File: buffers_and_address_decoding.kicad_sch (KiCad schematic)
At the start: 32 parts, among them U17 LS30, U18 74LS283, U19 LS04, U27 ADDR SELECT, U28 74LS283, U29 LS10, U3 81LS95, U30 LS20, U37 LS04, U38 LS10, U39 LS00, U4 LS04, U40 74LS42, U47 VECTOR FETCH ENAB, U7 LS30, U8 LS30

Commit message: First version of the schematic completed
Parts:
- U17: symbol 74LS30:74LS30_U17 -> LS_Logic:74LS30_U17
- U18, U28: symbol 74LS283:74LS283 -> LS_Logic:74LS283
- U3: symbol 81LS95:81LS95 -> LS_Logic:81LS95
- U37: footprint Package_DIP:DIP-14_W7.62mm_LongPads -> (none)
- U40: symbol 74LS42:74LS42_U40 -> LS_Logic:74LS42_U40
- U47: value VECTOR FETCH ENAB -> SYST
- U7: symbol 74LS30:74LS30_U7 -> LS_Logic:74LS30_U7
- U8: symbol 74LS30:74LS30_U8 -> LS_Logic:74LS30_U8
- renumbered R8 to R1, R3 to R10, R6 to R2, R4 to R3, R2 to R4, R5 to R7, R7 to R8, R1 to R9
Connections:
- net AB_0 renamed AB0
- net AB_1 renamed AB1
- net AB_10 renamed AB10
- net AB_11 renamed AB11
- net AB_12 renamed AB12
- net AB_13 renamed AB13
- net AB_14 renamed AB14
- net AB_15 renamed AB15
- net AB_2 renamed AB2
- net AB_3 renamed AB3
- net AB_4 renamed AB4
- net AB_5 renamed AB5
- net AB_6 renamed AB6
- net AB_7 renamed AB7
- net AB_8 renamed AB8
- net AB_9 renamed AB9
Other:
- note added: "VECTOR FETCH ENAB"
- note removed: "SYST"

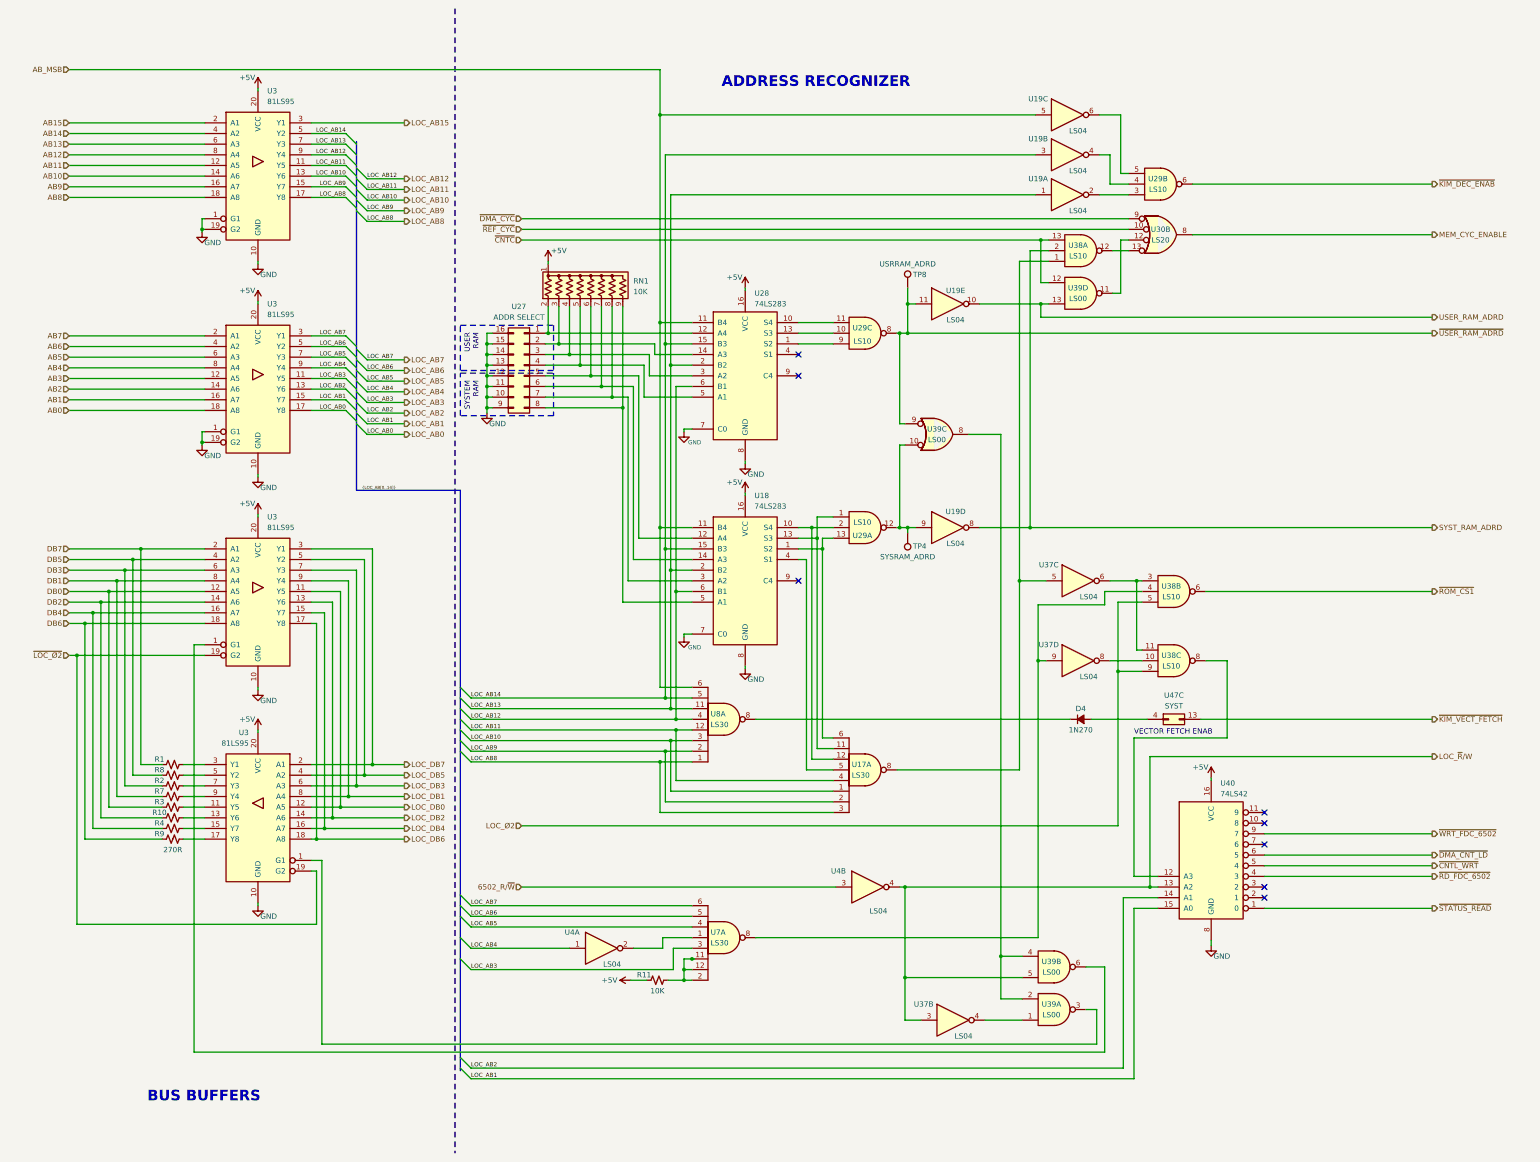
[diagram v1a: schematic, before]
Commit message: Schematic corrections
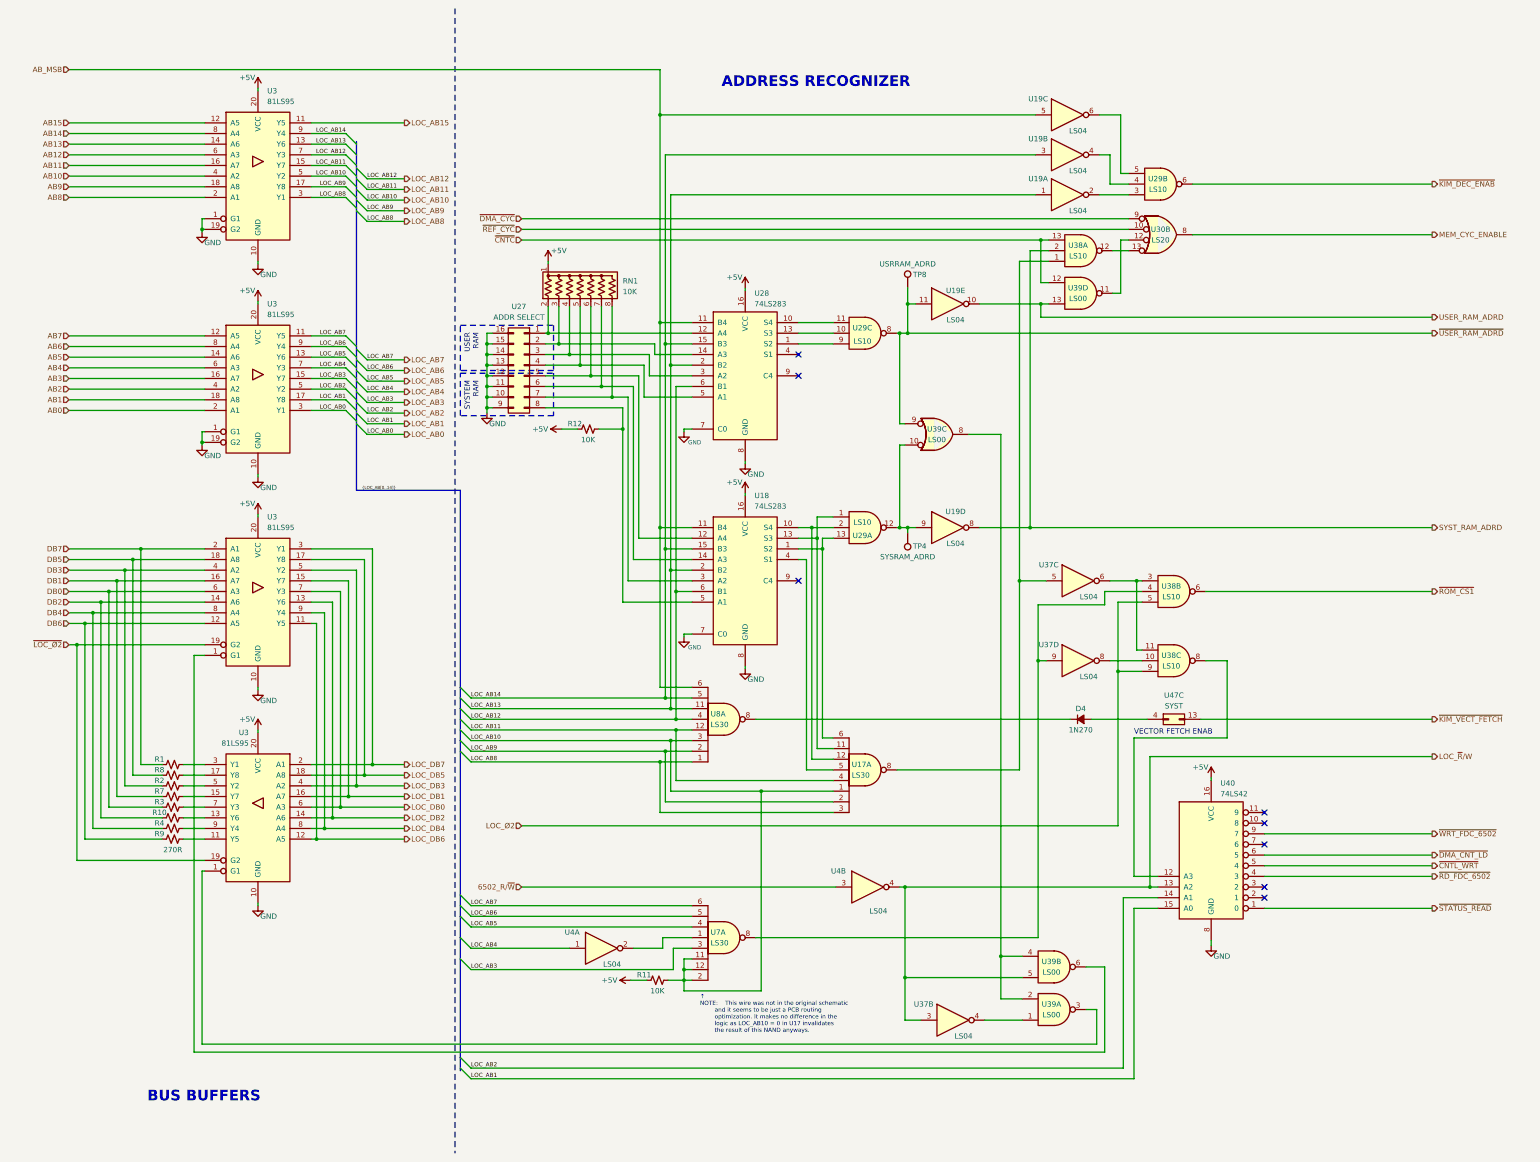
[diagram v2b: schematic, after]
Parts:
- added R12: 10K, K_1013_Jumper:R_Axial_DIN0204_L3.6mm_D2.5mm_P12.70mm_Horizontal, symbol Device:R_Small_US
- D4: footprint Diode_THT:D_DO-35_SOD27_P7.62mm_Horizontal -> K_1013_Jumper:D_DO-35_SOD27_P12.70mm_Horizontal
- R1, R10, R11, R2, R3, R4, R7, R8, R9: footprint Resistor_THT:R_Axial_DIN0207_L6.3mm_D2.5mm_P10.16mm_Horizontal -> K_1013_Jumper:R_Axial_DIN0204_L3.6mm_D2.5mm_P12.70mm_Horizontal
- RN1: footprint Resistor_THT:R_Array_SIP9 -> K_1013_Jumper:R_Array_SIP8; symbol Device:R_Network08_US -> Device:R_Network07_US
- TP4, TP8: footprint (none) -> K_1013_Jumper:TestPoint
- U17, U19, U29, U30, U38, U39, U4, U7, U8: footprint Package_DIP:DIP-14_W7.62mm_LongPads -> K_1013_Jumper:DIP-14_W7.62mm_LongPads
- U18, U27, U28, U47: footprint Package_DIP:DIP-16_W7.62mm_Socket_LongPads -> K_1013_Jumper:DIP-16_W7.62mm_LongPads
- U3: footprint Package_DIP:DIP-20_W7.62mm_LongPads -> K_1013_Jumper:DIP-20_W7.62mm_LongPads
- U3: footprint Package_DIP:DIP-20_W7.62mm_LongPads -> K_1013_Jumper:DIP-20_W7.62mm_LongPads; symbol LS_Logic:81LS95 -> LS_Logic:81LS95_U9
- U3: footprint Package_DIP:DIP-20_W7.62mm_LongPads -> K_1013_Jumper:DIP-20_W7.62mm_LongPads; symbol LS_Logic:81LS95 -> LS_Logic:81LS95_U3
- U37: footprint (none) -> K_1013_Jumper:DIP-14_W7.62mm_LongPads
- U40: footprint Package_DIP:DIP-16_W7.62mm_LongPads -> K_1013_Jumper:DIP-16_W7.62mm_LongPads
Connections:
- net +5V: now also R12.1
- net AB0: now also U3.2 (A1); no longer U3.18 (A8)
- net AB1: now also U3.18 (A8); no longer U3.16 (A7)
- net AB10: now also U3.4 (A2); no longer U3.14 (A6)
- net AB11: now also U3.16 (A7); no longer U3.12 (A5)
- net AB12: now also U3.6 (A3); no longer U3.8 (A4)
- net AB13: now also U3.14 (A6); no longer U3.6 (A3)
- net AB14: now also U3.8 (A4); no longer U3.4 (A2)
- net AB15: now also U3.12 (A5); no longer U3.2 (A1)
- net AB2: now also U3.4 (A2); no longer U3.14 (A6)
- net AB3: now also U3.16 (A7); no longer U3.12 (A5)
- net AB4: now also U3.6 (A3); no longer U3.8 (A4)
- net AB5: now also U3.14 (A6); no longer U3.6 (A3)
- net AB6: now also U3.8 (A4); no longer U3.4 (A2)
- net AB7: now also U3.12 (A5); no longer U3.2 (A1)
- net AB8: now also U3.2 (A1); no longer U3.18 (A8)
- net AB9: now also U3.18 (A8); no longer U3.16 (A7)
- net DB0: now also U3.6 (A3); no longer U3.12 (A5)
- net DB1: now also U3.16 (A7); no longer U3.8 (A4)
- net DB3: now also U3.4 (A2); no longer U3.6 (A3)
- net DB4: now also U3.8 (A4); no longer U3.16 (A7)
- net DB5: now also U3.18 (A8); no longer U3.4 (A2)
- net DB6: now also U3.12 (A5); no longer U3.18 (A8)
- net LOC_AB0: now also U3.3 (Y1); no longer U3.17 (Y8)
- net LOC_AB1: now also U3.17 (Y8); no longer U3.15 (Y7)
- net LOC_AB10: now also R11.2, U3.5 (Y2), U7.11, U7.12, U7.2; no longer U3.13 (Y6)
- net LOC_AB11: now also U3.15 (Y7); no longer U3.11 (Y5)
- net LOC_AB12: now also U3.7 (Y3); no longer U3.9 (Y4)
- net LOC_AB13: now also U3.13 (Y6); no longer U3.7 (Y3)
- net LOC_AB14: now also U3.9 (Y4); no longer U3.5 (Y2)
- net LOC_AB15: now also U3.11 (Y5); no longer U3.3 (Y1)
- net LOC_AB2: now also U3.5 (Y2); no longer U3.13 (Y6)
- net LOC_AB3: now also U3.15 (Y7); no longer U3.11 (Y5)
- net LOC_AB4: now also U3.7 (Y3); no longer U3.9 (Y4)
- net LOC_AB5: now also U3.13 (Y6); no longer U3.7 (Y3)
- net LOC_AB6: now also U3.9 (Y4); no longer U3.5 (Y2)
- net LOC_AB7: now also U3.11 (Y5); no longer U3.3 (Y1)
- net LOC_AB8: now also U3.3 (Y1); no longer U3.17 (Y8)
- net LOC_AB9: now also U3.17 (Y8); no longer U3.15 (Y7)
- net LOC_DB0: now also U3.6 (A3), U3.7 (Y3); no longer U3.11 (Y5), U3.12 (A5)
- net LOC_DB1: now also U3.15 (Y7), U3.16 (A7); no longer U3.8 (A4), U3.9 (Y4)
- net LOC_DB3: now also U3.4 (A2), U3.5 (Y2); no longer U3.6 (A3), U3.7 (Y3)
- net LOC_DB4: now also U3.8 (A4), U3.9 (Y4); no longer U3.15 (Y7), U3.16 (A7)
- net LOC_DB5: now also U3.17 (Y8), U3.18 (A8); no longer U3.4 (A2), U3.5 (Y2)
- net LOC_DB6: now also U3.11 (Y5), U3.12 (A5); no longer U3.17 (Y8), U3.18 (A8)
- net at R7.2: now also U3.15 (Y7); no longer U3.9 (Y4)
- net at R8.2: now also U3.17 (Y8); no longer U3.5 (Y2)
- net at U18.5 (A1), U27.8 (Pin_8): now also R12.2; no longer RN1.9 (R8)
- net at U3.11 (Y5): now also R9.2; no longer R3.2
- net at R4.2: now also U3.9 (Y4); no longer U3.15 (Y7)
- net at R2.2: now also U3.5 (Y2); no longer U3.7 (Y3)
- new net: R3.2, U3.7 (Y3)
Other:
- note added: "↑ NOTE: This wire was not in the original schematic and it seems to be just a PCB routing optimization. It makes no difference in the logic as LOC_AB10 = 0 in U17 invalidates the result of this NAND anyways."

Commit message: Update progress
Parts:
- D4: footprint K_1013_Jumper:D_DO-35_SOD27_P12.70mm_Horizontal -> K_1013:D_DO-35_SOD27_P12.70mm_Horizontal
- R1, R10, R11, R12, R2, R3, R4, R7, R8, R9: footprint K_1013_Jumper:R_Axial_DIN0204_L3.6mm_D2.5mm_P12.70mm_Horizontal -> K_1013:R_Axial_DIN0204_L3.6mm_D2.5mm_P12.70mm_Horizontal
- RN1: footprint K_1013_Jumper:R_Array_SIP8 -> K_1013:R_Array_SIP8
- TP4, TP8: footprint K_1013_Jumper:TestPoint -> K_1013:TestPoint
- U17, U29, U30, U37, U38, U39, U4, U7, U8: footprint K_1013_Jumper:DIP-14_W7.62mm_LongPads -> K_1013:DIP-14_W7.62mm_LongPads
- U18, U27, U28, U40, U47: footprint K_1013_Jumper:DIP-16_W7.62mm_LongPads -> K_1013:DIP-16_W7.62mm_LongPads
- U19: footprint K_1013_Jumper:DIP-14_W7.62mm_LongPads -> K_1013:DIP-14_W7.62mm_LongPads_U19
- U3: footprint K_1013_Jumper:DIP-20_W7.62mm_LongPads -> K_1013:DIP-20_W7.62mm_LongPads; symbol LS_Logic:81LS95 -> LS_Logic:81LS95_U1_U2
- U3: footprint K_1013_Jumper:DIP-20_W7.62mm_LongPads -> K_1013:DIP-20_W7.62mm_LongPads_U9
- U3: footprint K_1013_Jumper:DIP-20_W7.62mm_LongPads -> K_1013:DIP-20_W7.62mm_LongPads
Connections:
- net DB0: now also R9.1, U3.12 (A5); no longer R3.1, U3.6 (A3)
- net DB1: now also R4.1, U3.8 (A4); no longer R7.1, U3.16 (A7)
- net DB3: now also R3.1, U3.6 (A3); no longer R2.1, U3.4 (A2)
- net DB4: now also R7.1, U3.16 (A7); no longer R4.1, U3.8 (A4)
- net DB5: now also R2.1, U3.4 (A2); no longer R8.1, U3.18 (A8)
- net DB6: now also R8.1, U3.18 (A8); no longer R9.1, U3.12 (A5)
- net LOC_DB0: now also U3.11 (Y5), U3.12 (A5); no longer U3.6 (A3), U3.7 (Y3)
- net LOC_DB1: now also U3.8 (A4), U3.9 (Y4); no longer U3.15 (Y7), U3.16 (A7)
- net LOC_DB3: now also U3.6 (A3), U3.7 (Y3); no longer U3.4 (A2), U3.5 (Y2)
- net LOC_DB4: now also U3.15 (Y7), U3.16 (A7); no longer U3.8 (A4), U3.9 (Y4)
- net LOC_DB5: now also U3.4 (A2), U3.5 (Y2); no longer U3.17 (Y8), U3.18 (A8)
- net LOC_DB6: now also U3.17 (Y8), U3.18 (A8); no longer U3.11 (Y5), U3.12 (A5)

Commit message: Routing of the bottom layer completed
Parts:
- U17: footprint K_1013:DIP-14_W7.62mm_LongPads -> K_1013:DIP-14_W7.62mm_LongPads_U17
- U30: footprint K_1013:DIP-14_W7.62mm_LongPads -> K_1013:DIP-14_W7.62mm_LongPads_U30
- U37: footprint K_1013:DIP-14_W7.62mm_LongPads -> K_1013:DIP-14_W7.62mm_LongPads_U37
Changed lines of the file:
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@@
       (effects (font (size 1.27 1.27)))
     )
-    (property "Footprint" "K_1013:DIP-14_W7.62mm_LongPads" (at 280.035 148.59 0)
+    (property "Footprint" "K_1013:DIP-14_W7.62mm_LongPads_U37" (at 280.035 148.59 0)
       (effects (font (size 1.27 1.27)) hide)
     )
@@
       (effects (font (size 1.27 1.27)))
     )
-    (property "Footprint" "K_1013:DIP-14_W7.62mm_LongPads" (at 299.72 66.04 0)
+    (property "Footprint" "K_1013:DIP-14_W7.62mm_LongPads_U30" (at 299.72 66.04 0)
       (effects (font (size 1.27 1.27)) hide)
     )
@@
       (effects (font (size 1.27 1.27)) (justify left))
     )
-    (property "Footprint" "K_1013:DIP-14_W7.62mm_LongPads" (at 229.235 193.675 0)
+    (property "Footprint" "K_1013:DIP-14_W7.62mm_LongPads_U17" (at 229.235 193.675 0)
       (effects (font (size 1.27 1.27)) hide)
     )
@@
       (effects (font (size 1.27 1.27)))
     )
-    (property "Footprint" "K_1013:DIP-14_W7.62mm_LongPads" (at 280.035 167.64 0)
+    (property "Footprint" "K_1013:DIP-14_W7.62mm_LongPads_U37" (at 280.035 167.64 0)
       (effects (font (size 1.27 1.27)) hide)
     )
@@
       (effects (font (size 1.27 1.27)))
     )
-    (property "Footprint" "K_1013:DIP-14_W7.62mm_LongPads" (at 250.19 253.365 0)
-      (effects (font (size 1.27 1.27)) hide)
-    )
+    (property "Footprint" "K_1013:DIP-14_W7.62mm_LongPads_U37" (at 250.19 253.365 0)
+      (effects (font (size 1.27 1.27)) hide)
+    )

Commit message: Completed first version of board routing
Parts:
- R1, R10, R2, R3, R4, R7, R8, R9: footprint K_1013:R_Axial_DIN0204_L3.6mm_D2.5mm_P12.70mm_Horizontal -> K_1013:R_Axial_DIN0204_L3.6mm_D2.5mm_P12.70mm_Horizontal_270R
- R11, R12: footprint K_1013:R_Axial_DIN0204_L3.6mm_D2.5mm_P12.70mm_Horizontal -> K_1013:R_Axial_DIN0204_L3.6mm_D2.5mm_P12.70mm_Horizontal_10K
- U27, U47: footprint K_1013:DIP-16_W7.62mm_LongPads -> K_1013:DIP-16_W7.62mm_LongPads_SW
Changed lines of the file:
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@@
       (effects (font (size 1.27 1.27)) hide)
     )
-    (property "Footprint" "K_1013:R_Axial_DIN0204_L3.6mm_D2.5mm_P12.70mm_Horizontal" (at 64.135 200.025 0)
+    (property "Footprint" "K_1013:R_Axial_DIN0204_L3.6mm_D2.5mm_P12.70mm_Horizontal_270R" (at 64.135 200.025 0)
       (effects (font (size 1.27 1.27)) hide)
     )
@@
       (effects (font (size 1.27 1.27)) hide)
     )
-    (property "Footprint" "K_1013:R_Axial_DIN0204_L3.6mm_D2.5mm_P12.70mm_Horizontal" (at 64.135 194.945 0)
+    (property "Footprint" "K_1013:R_Axial_DIN0204_L3.6mm_D2.5mm_P12.70mm_Horizontal_270R" (at 64.135 194.945 0)
       (effects (font (size 1.27 1.27)) hide)
     )
@@
       (effects (font (size 1.27 1.27)) hide)
     )
-    (property "Footprint" "K_1013:R_Axial_DIN0204_L3.6mm_D2.5mm_P12.70mm_Horizontal" (at 64.135 197.485 0)
+    (property "Footprint" "K_1013:R_Axial_DIN0204_L3.6mm_D2.5mm_P12.70mm_Horizontal_270R" (at 64.135 197.485 0)
       (effects (font (size 1.27 1.27)) hide)
     )
@@
       (effects (font (size 1.27 1.27)))
     )
-    (property "Footprint" "K_1013:R_Axial_DIN0204_L3.6mm_D2.5mm_P12.70mm_Horizontal" (at 179.705 243.84 0)
+    (property "Footprint" "K_1013:R_Axial_DIN0204_L3.6mm_D2.5mm_P12.70mm_Horizontal_10K" (at 179.705 243.84 0)
       (effects (font (size 1.27 1.27)) hide)
     )
@@
       (effects (font (size 1.27 1.27)) hide)
     )
-    (property "Footprint" "K_1013:R_Axial_DIN0204_L3.6mm_D2.5mm_P12.70mm_Horizontal" (at 64.135 205.105 0)
+    (property "Footprint" "K_1013:R_Axial_DIN0204_L3.6mm_D2.5mm_P12.70mm_Horizontal_270R" (at 64.135 205.105 0)
       (effects (font (size 1.27 1.27)) hide)
     )
@@
       (effects (font (size 1.27 1.27)))
     )
-    (property "Footprint" "K_1013:DIP-16_W7.62mm_LongPads" (at 147.955 97.155 0)
+    (property "Footprint" "K_1013:DIP-16_W7.62mm_LongPads_SW" (at 147.955 97.155 0)
       (effects (font (size 1.27 1.27)) hide)
     )
@@
       (effects (font (size 1.27 1.27)) hide)
     )
-    (property "Footprint" "K_1013:R_Axial_DIN0204_L3.6mm_D2.5mm_P12.70mm_Horizontal" (at 64.135 202.565 0)
+    (property "Footprint" "K_1013:R_Axial_DIN0204_L3.6mm_D2.5mm_P12.70mm_Horizontal_270R" (at 64.135 202.565 0)
       (effects (font (size 1.27 1.27)) hide)
     )
@@
       (effects (font (size 1.27 1.27)))
     )
-    (property "Footprint" "K_1013:R_Axial_DIN0204_L3.6mm_D2.5mm_P12.70mm_Horizontal" (at 163.195 112.395 0)
+    (property "Footprint" "K_1013:R_Axial_DIN0204_L3.6mm_D2.5mm_P12.70mm_Horizontal_10K" (at 163.195 112.395 0)
       (effects (font (size 1.27 1.27)) hide)
     )
@@
       (effects (font (size 1.27 1.27)) hide)
     )
-    (property "Footprint" "K_1013:R_Axial_DIN0204_L3.6mm_D2.5mm_P12.70mm_Horizontal" (at 64.135 207.645 0)
+    (property "Footprint" "K_1013:R_Axial_DIN0204_L3.6mm_D2.5mm_P12.70mm_Horizontal_270R" (at 64.135 207.645 0)
       (effects (font (size 1.27 1.27)) hide)
     )
@@
       (effects (font (size 1.27 1.27)))
     )
-    (property "Footprint" "K_1013:R_Axial_DIN0204_L3.6mm_D2.5mm_P12.70mm_Horizontal" (at 64.135 210.185 0)
+    (property "Footprint" "K_1013:R_Axial_DIN0204_L3.6mm_D2.5mm_P12.70mm_Horizontal_270R" (at 64.135 210.185 0)
       (effects (font (size 1.27 1.27)) hide)
     )
@@
       (effects (font (size 1.27 1.27)) hide)
     )
-    (property "Footprint" "K_1013:R_Axial_DIN0204_L3.6mm_D2.5mm_P12.70mm_Horizontal" (at 64.135 192.405 0)
+    (property "Footprint" "K_1013:R_Axial_DIN0204_L3.6mm_D2.5mm_P12.70mm_Horizontal_270R" (at 64.135 192.405 0)
       (effects (font (size 1.27 1.27)) hide)
     )
@@
       (effects (font (size 1.27 1.27)))
     )
-    (property "Footprint" "K_1013:DIP-16_W7.62mm_LongPads" (at 301.625 181.61 0)
-      (effects (font (size 1.27 1.27)) hide)
-    )
+    (property "Footprint" "K_1013:DIP-16_W7.62mm_LongPads_SW" (at 301.625 181.61 0)
+      (effects (font (size 1.27 1.27)) hide)
+    )

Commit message: Cosmetic changes
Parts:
- U30: symbol 74xx:74LS20 -> LS_Logic:74LS20_U30
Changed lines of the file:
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@@
     )
   )
-  (symbol (lib_id "LS_Logic:81LS95_U1_U2") (at 84.455 52.07 0) (unit 1)
+  (symbol (lib_name "81LS95_U1_U2_1") (lib_id "LS_Logic:81LS95_U1_U2") (at 84.455 52.07 0) (unit 1)
     (in_bom yes) (on_board yes) (dnp no)
     (property "Reference" "U3" (at 86.6491 31.75 0)
@@
     (pin "7")
     (pin "11")
+    (pin "10")
+    (pin "9")
+    (pin "13")
     (instances
       (project "k-1013-floppy-controller-replica"
@@
     )
   )
-  (symbol (lib_id "74xx:74LS20") (at 299.72 66.04 0) (unit 2) (convert 2)
+  (symbol (lib_id "LS_Logic:74LS20_U30") (at 299.72 66.04 0) (unit 2) (convert 2)
     (in_bom yes) (on_board yes) (dnp no)
     (property "Reference" "U30" (at 299.72 64.77 0)
@@
     (pin "7")
     (pin "2")
+    (pin "11")
     (instances
       (project "k-1013-floppy-controller-replica"
@@
     (pin "6")
     (pin "1")
+    (pin "10")
+    (pin "9")
+    (pin "13")
     (instances
       (project "k-1013-floppy-controller-replica"
@@
     (pin "9")
     (pin "10")
-    (instances
-      (project "k-1013-floppy-controller-replica"
+    (pin "13")
+    (instances
+      (project "k-1013-floppy-controller-replica"
